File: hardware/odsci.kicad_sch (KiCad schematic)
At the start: 0 parts

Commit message: hardware: schematic completed
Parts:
- added C1: 1uF, Capacitor_SMD:C_0805_2012Metric, symbol Device:C
- added C10, C8: 4.7uF, Capacitor_SMD:C_0805_2012Metric, symbol Device:C
- added C2: 10uF, Capacitor_SMD:C_0805_2012Metric, symbol Device:C
- added C3, C4, C5, C6, C7, C9: 100nF, Capacitor_SMD:C_0402_1005Metric, symbol Device:C
- added D1, D2, D3: LED, LED_THT:LED_D3.0mm, symbol Device:LED
- added J1: USB_C_Receptacle, Connector_USB:USB_C_Receptacle_Amphenol_12401610E4-2A, symbol Connector:USB_C_Receptacle
- added J2: Conn_01x03_Pin, Connector_PinHeader_2.54mm:PinHeader_1x03_P2.54mm_Vertical, symbol Connector:Conn_01x03_Pin
- added J3: Conn_01x04_Pin, Connector_PinHeader_2.54mm:PinHeader_1x04_P2.54mm_Vertical, symbol Connector:Conn_01x04_Pin
- added J4: Screw_Terminal_01x03, TerminalBlock_Phoenix:TerminalBlock_Phoenix_MPT-0,5-3-2.54_1x03_P2.54mm_Horizontal, symbol Connector:Screw_Terminal_01x03
- added R1, R2: 5.1k, Resistor_SMD:R_0402_1005Metric, symbol Device:R
- added R3, R4: 10k, Resistor_SMD:R_0402_1005Metric, symbol Device:R
- added R5: 4.7k, Resistor_SMD:R_0402_1005Metric, symbol Device:R
- added R6, R7, R8: 330, Resistor_SMD:R_0402_1005Metric, symbol Device:R
- added SW1: SW_Push, symbol Switch:SW_Push
- added U1: TPS7A4701xRGW, Package_DFN_QFN:Texas_RGW0020A_VQFN-20-1EP_5x5mm_P0.65mm_EP3.15x3.15mm_ThermalVias, symbol Regulator_Linear:TPS7A4701xRGW
- added U2: STM32F042K6Tx, Package_QFP:LQFP-32_7x7mm_P0.8mm, symbol MCU_ST_STM32F0:STM32F042K6Tx
- added U3: USBLC6-2SC6, Package_TO_SOT_SMD:SOT-23-6, symbol Power_Protection:USBLC6-2SC6
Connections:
- new net: D1.2 (A), R6.1
- new net: C1.2, U1.14 (NR)
- new net: J1.A5 (CC1), R1.1
- new net: J1.A6 (D+), J1.B6 (D+), U3.3 (I/O2)
- new net: J1.A7 (D-), J1.B7 (D-), U3.1 (I/O1)
- new net: J1.B5 (CC2), R2.1
- new net: C7.1, R4.1, SW1.2, U2.31 (PB8)
- new net: D3.2 (A), R8.1
- new net: C6.1, R3.1, U2.4 (NRST)
- new net: D2.2 (A), R7.1
- new net ACTIVITY_LED: R7.2, U2.12 (PA6)
- new net CAPTURE_LED: R8.2, U2.13 (PA7)
- new net GND: C1.1, C10.2, C2.1, C3.1, C4.1, C5.1, C6.2, C7.2, C8.1, C9.1, D1.1 (K), D2.1 (K), D3.1 (K), J1.A1 (GND), J1.A12 (GND), J1.B1 (GND), J1.B12 (GND), J1.S1 (SHIELD), J2.1 (Pin_1), J3.1 (Pin_1), J4.3 (Pin_3), R1.2, R2.2, R4.2, U1.11 (0.2V), U1.12 (0.1V), U1.21 (EP), U1.7 (GND), U1.8 (1.6V), U2.16 (VSS), U2.32 (VSSA), U3.2 (GND)
- new net ONEWIRE_BUS: J4.2 (Pin_2), R5.1, U2.28 (PB5)
- new net SWCLK_PA14: J3.4 (Pin_4), U2.24 (PA14)
- new net SWDIO_PA13: J3.3 (Pin_3), U2.23 (PA13)
- new net USB_D_NEGATIVE: U2.21 (PA11), U3.6 (I/O1)
- new net USB_D_POSITIVE: U2.22 (PA12), U3.4 (I/O2)
- new net VBUS: C10.1, C2.2, C9.2, J1.A4 (VBUS), J1.A9 (VBUS), J1.B4 (VBUS), J1.B9 (VBUS), J2.2 (Pin_2), U1.13 (EN), U1.15 (IN), U1.16 (IN), U3.5 (VBUS)
- new net VDD: C3.2, C4.2, C5.2, C8.2, J2.3 (Pin_3), J3.2 (Pin_2), J4.1 (Pin_1), R3.2, R5.2, R6.2, SW1.1, U1.1 (OUT), U1.20 (OUT), U1.3 (SENSE/FB), U2.1 (VDD), U2.17 (VDDIO2), U2.5 (VDDA)
- no-connect marks 0 -> 33
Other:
- note added: "DS18B20 Terminal"
- note added: "ESD Protection"
- note added: "LED Indicators"
- note added: "STM32"
- note added: "SWD Header"
- note added: "USB-C Port"
- note added: "Voltage Regulation"
- note added: "Voltage Test Headers"
- company: (none) -> Stratos Thivaios - sthivaios.dev
- title: (none) -> ODSCI

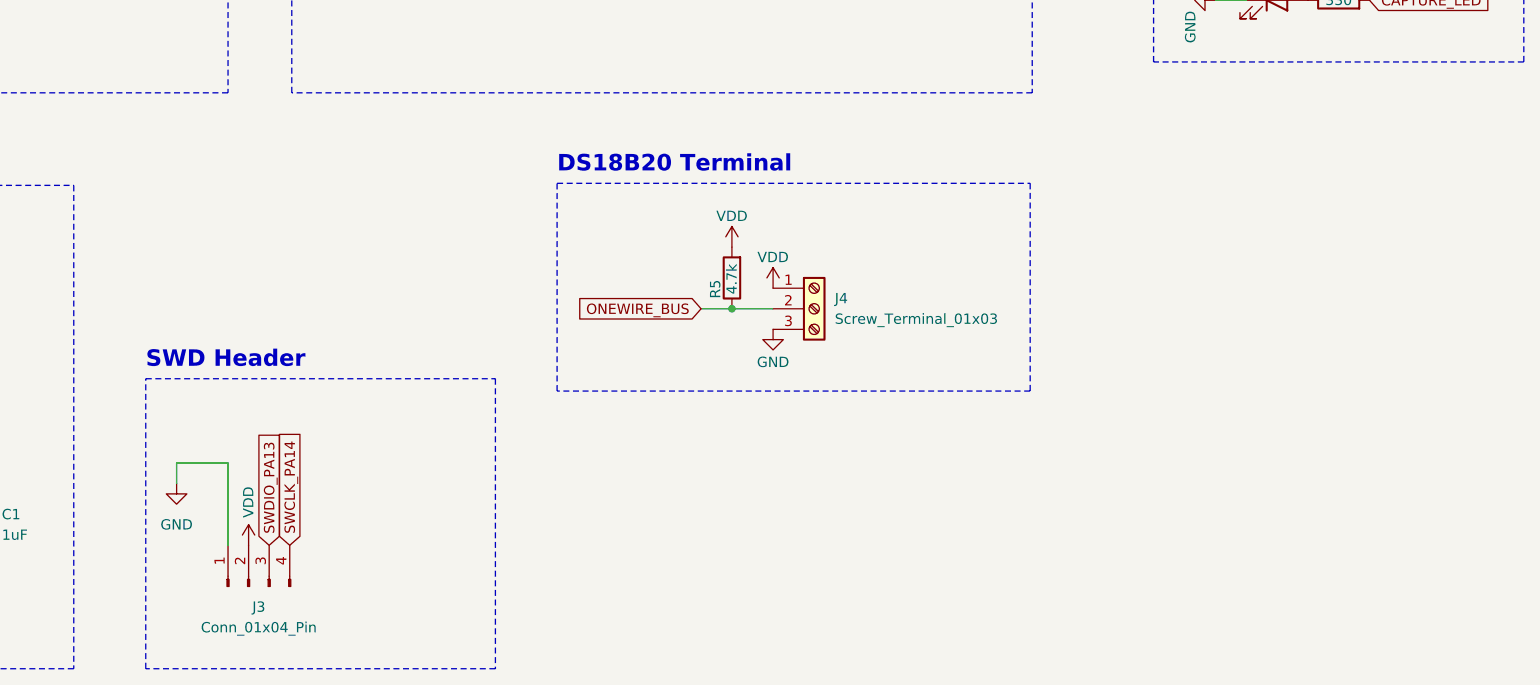
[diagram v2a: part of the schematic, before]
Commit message: hardware: add mounting holes to pcb
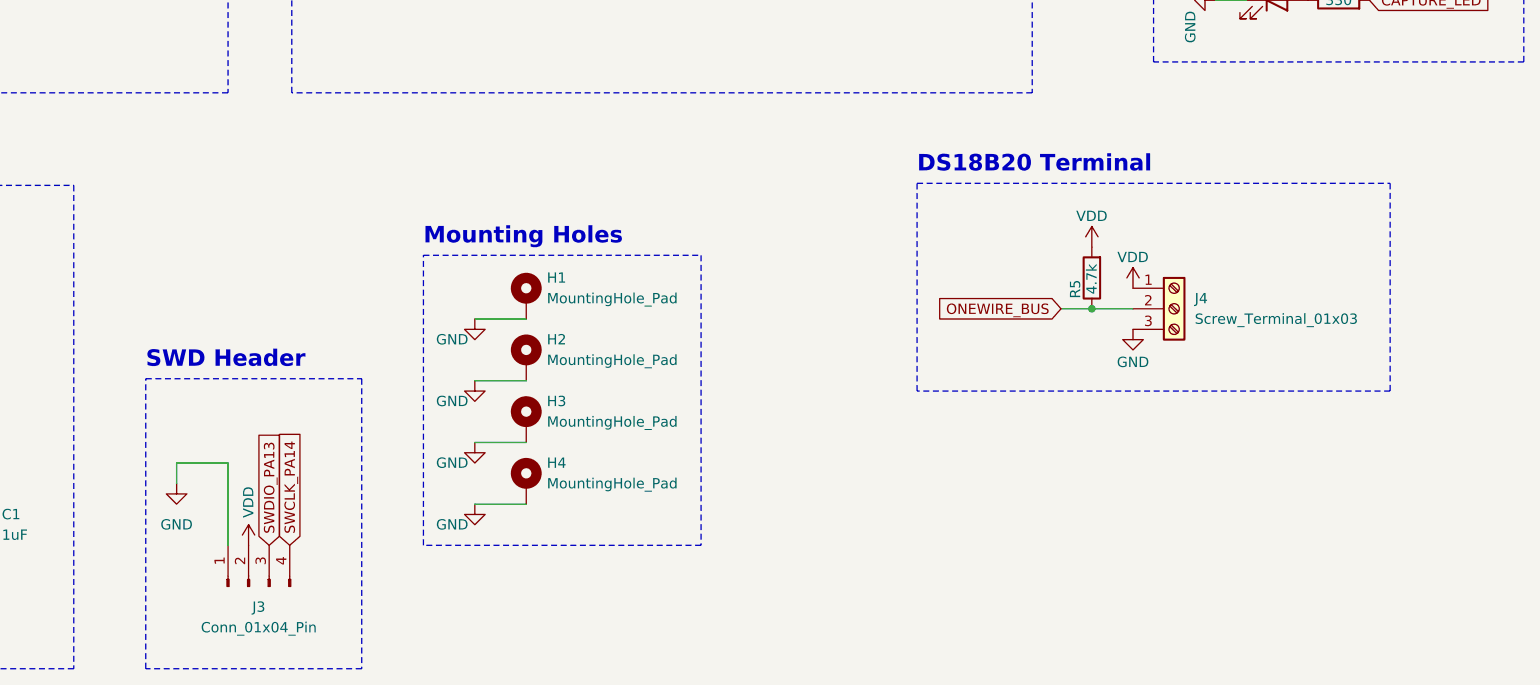
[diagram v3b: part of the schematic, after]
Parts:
- added H1, H2, H3, H4: MountingHole_Pad, MountingHole:MountingHole_2.2mm_M2_Pad, symbol Mechanical:MountingHole_Pad
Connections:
- net GND: now also H1.1, H2.1, H3.1, H4.1
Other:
- note added: "Mounting Holes"
- moved on the sheet: J4, R5

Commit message: hardware: add a few decoupling caps
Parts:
- added C11: 47uF, Capacitor_SMD:C_0805_2012Metric, symbol Device:C
- added C12: 4.7uF, Capacitor_SMD:C_0805_2012Metric, symbol Device:C
- SW1: footprint (none) -> Button_Switch_THT:SW_SPST_Omron_B3F-315x_Angled
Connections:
- net GND: now also C11.2, C12.2
- net VDD: now also C11.1, C12.1
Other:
- moved on the sheet: J4, R5

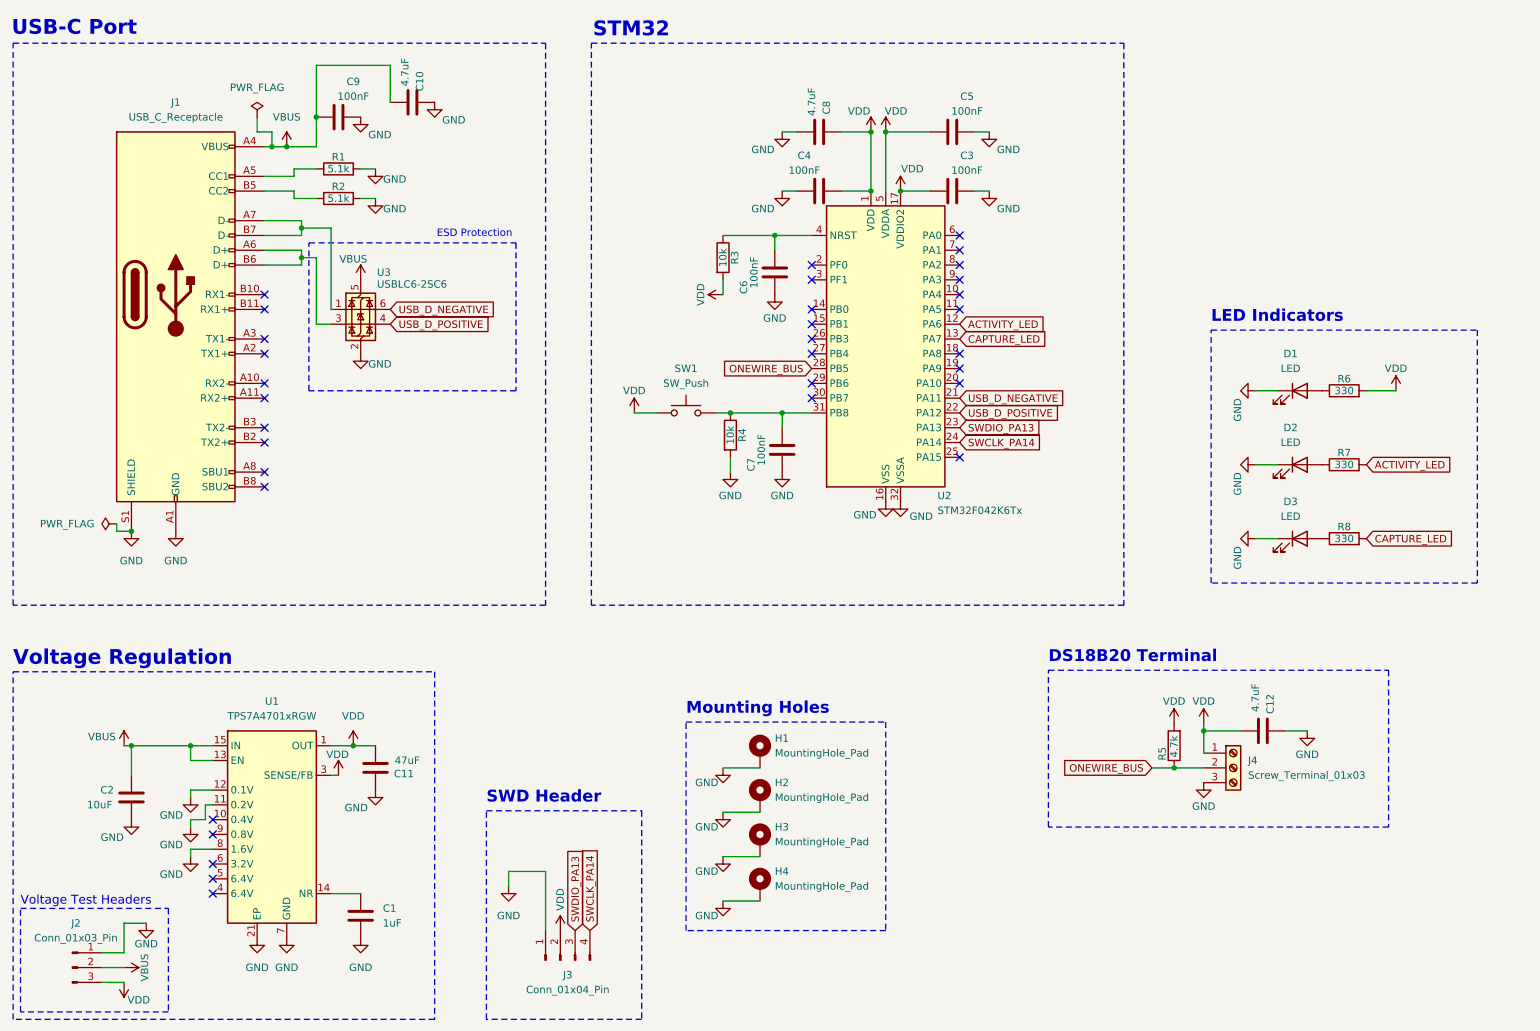
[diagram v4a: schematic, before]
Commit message: hardware: fully reroute and change pcb's layout
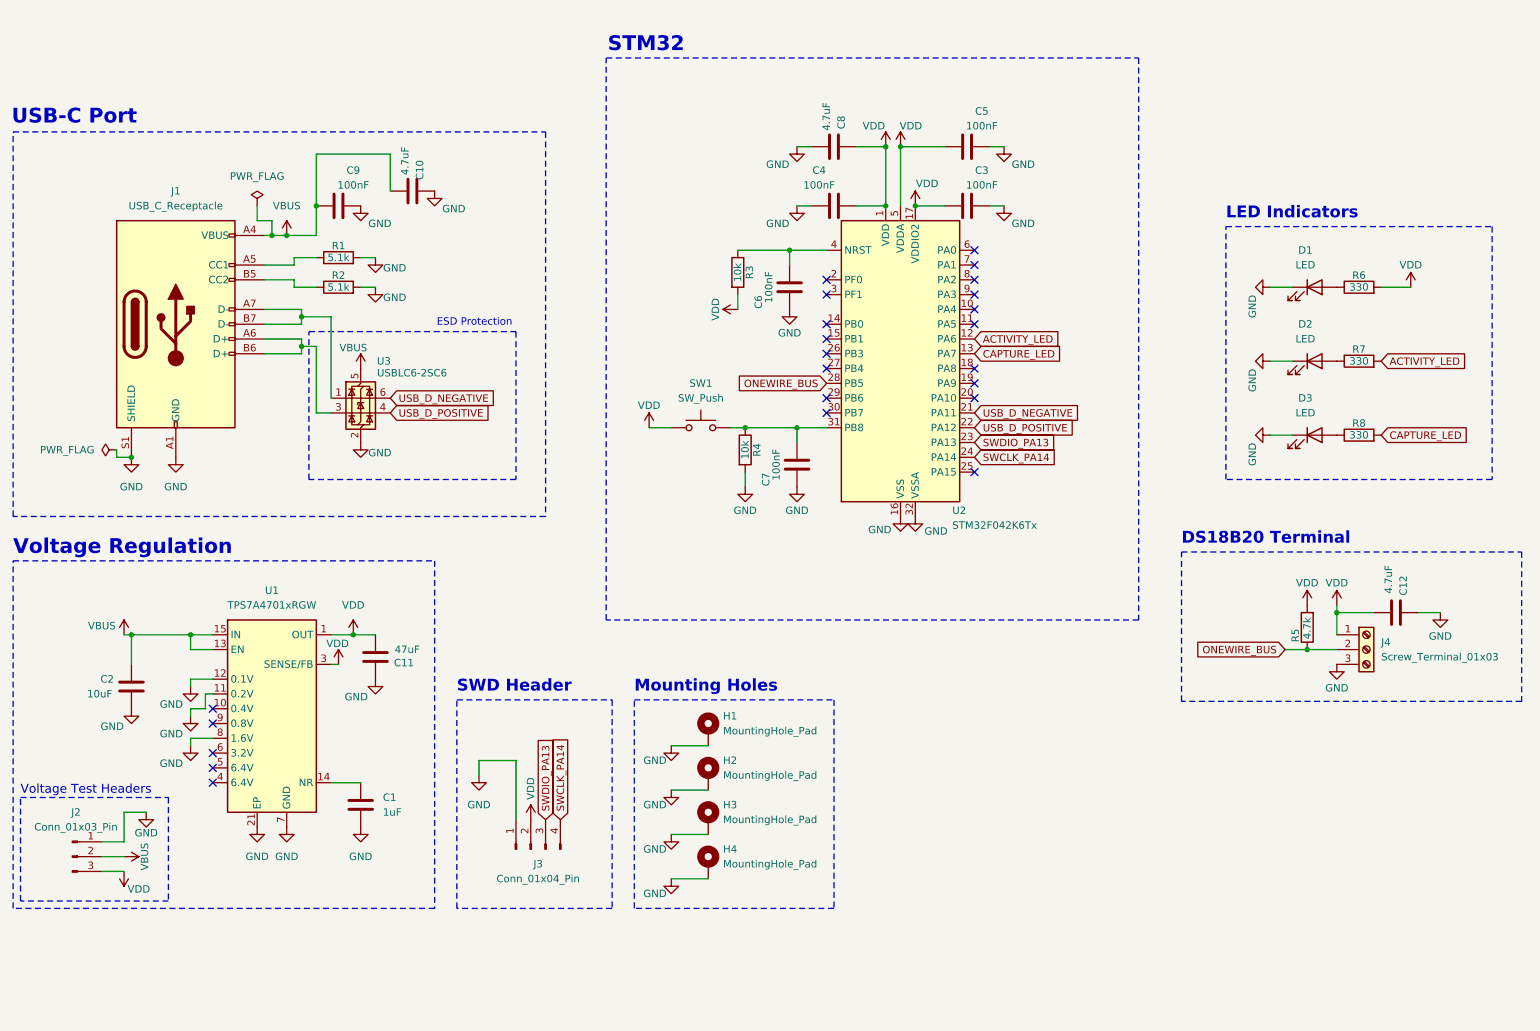
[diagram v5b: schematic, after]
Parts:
- J1: footprint Connector_USB:USB_C_Receptacle_Amphenol_12401610E4-2A -> Connector_USB:USB_C_Receptacle_GCT_USB4105-xx-A_16P_TopMnt_Horizontal; symbol Connector:USB_C_Receptacle -> Connector:USB_C_Receptacle_USB2.0_14P
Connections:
- no-connect marks 33 -> 23
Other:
- moved on the sheet: C1, C10, C11, C12, C2, C3, C4, C5, C6, C7, C8, C9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

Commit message: hardware and schematic: add LCSC part number for switch
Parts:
- SW1: LCSC (none) -> C231320
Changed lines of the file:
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@@
+			)
+		)
+		(property "LCSC" "C231320"
+			(at 138.43 90.17 0)
+			(effects
+				(font
+					(size 1.27 1.27)
+				)
+				(hide yes)
 			)
 		)

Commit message: hardware and schematic: update USB-C connector LCSC part number
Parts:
- J1: LCSC C5119948 -> C3020560
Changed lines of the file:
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@@
 			)
 		)
-		(property "LCSC" "C5119948"
+		(property "LCSC" "C3020560"
 			(at 48.26 72.39 0)
 			(effects

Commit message: hardware and schematic: update STM32 LCSC part number
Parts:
- U2: LCSC C1337340 -> C69216
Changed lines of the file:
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@@
 			)
 		)
-		(property "LCSC" "C1337340"
+		(property "LCSC" "C69216"
 			(at 172.72 80.01 0)
 			(effects
